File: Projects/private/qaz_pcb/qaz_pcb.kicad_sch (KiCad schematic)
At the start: 77 parts, among them U1 Frood

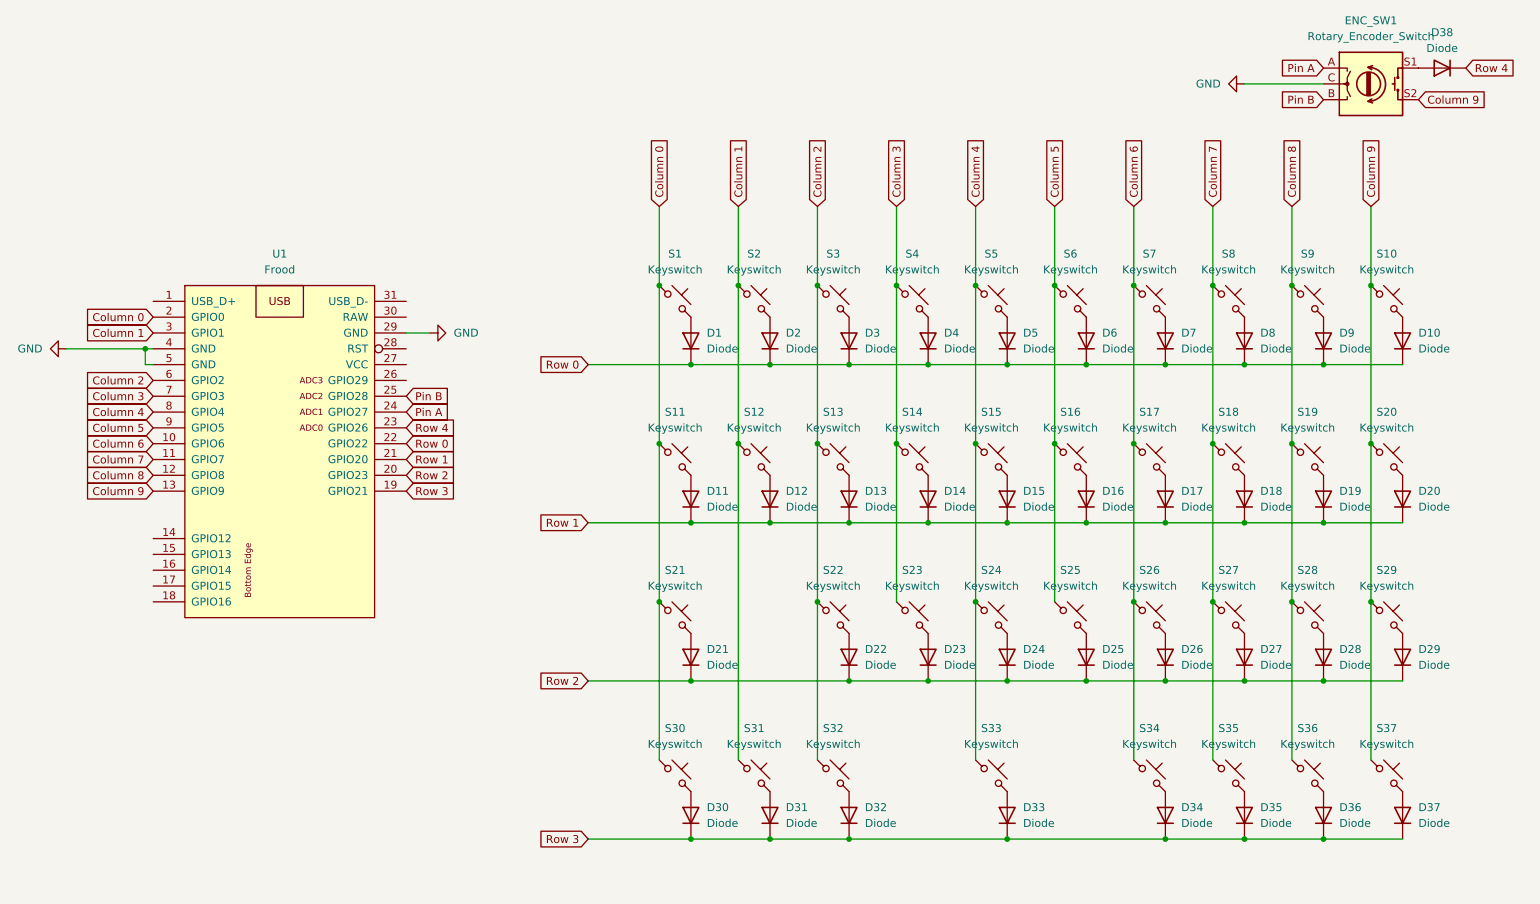
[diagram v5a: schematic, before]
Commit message: Major update
- renamed everything from 'scottokeebs' and 'kunsteak' to 'personal' for easier access and personalisation/individualisation.
- updated README to include sources used in QAZ project
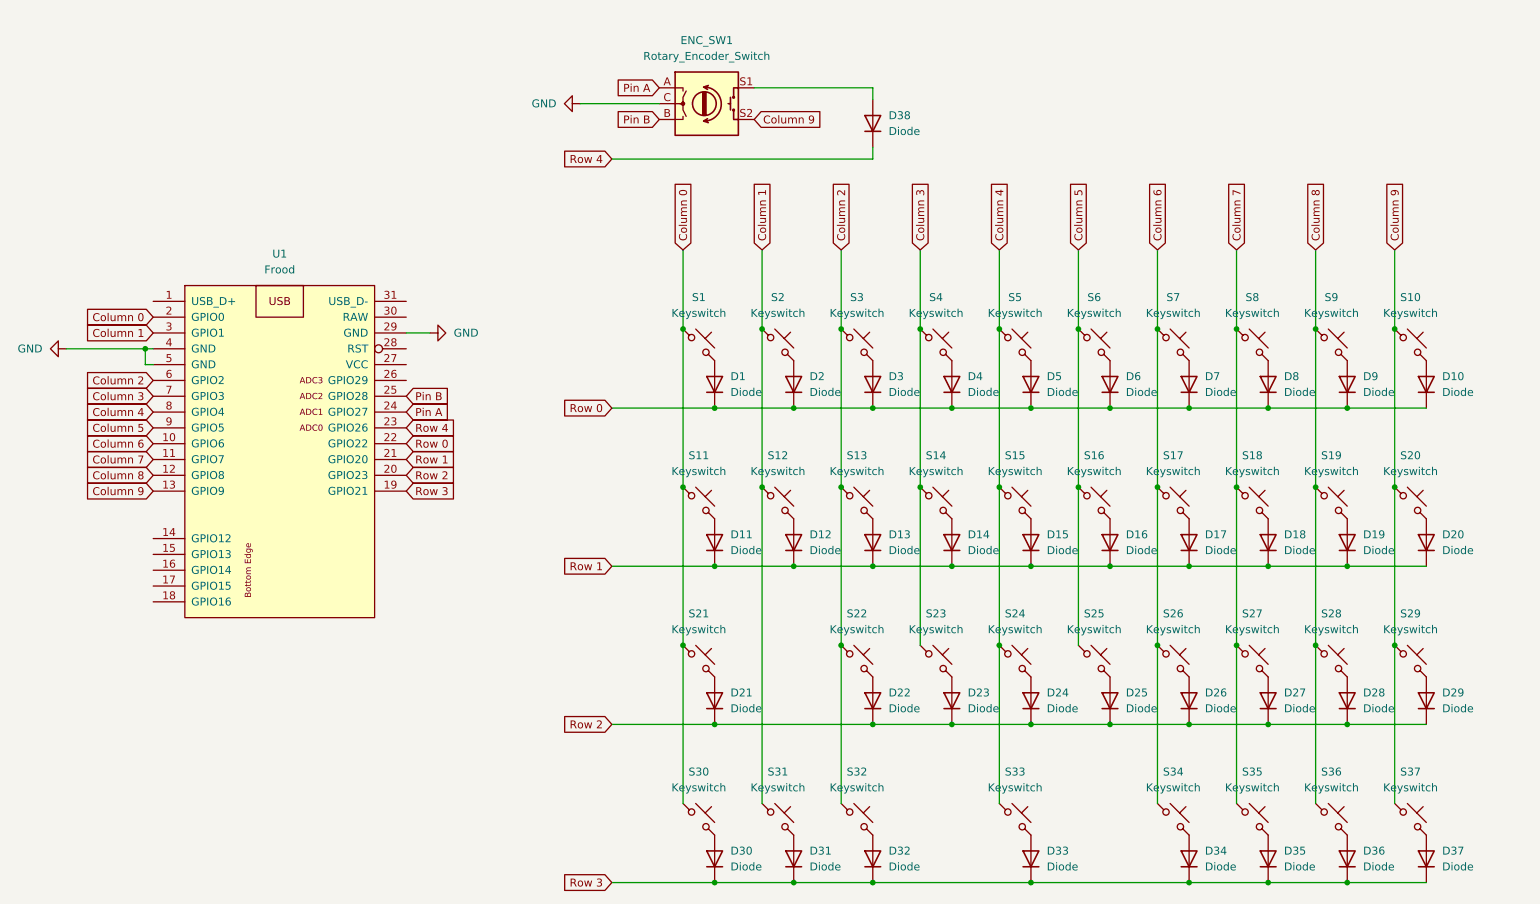
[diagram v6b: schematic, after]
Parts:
- D1, D10, D11, D12, D13, D14, D15, D16, D17, D18, D19, D2, D20, D21, D22, D23, D24, D25, D26, D27, D28, D29, D3, D30, D31, D32, D33, D34, D35, D36, D37, D38, D4, D5, D6, D7, D8, D9: footprint Kunsteak_Components:Diode_SOD-123 -> Personal_Components:Diode_SOD-123; symbol Kunsteak:Placeholder_Diode -> Personal:Placeholder_Diode
- ENC_SW1: footprint Kunsteak_Components:Rotary_Encoder_PEC11R-4220K-S0024 -> Personal_Components:Rotary_Encoder_PEC11R-4220K-S0024; symbol ScottoKeebs:Rotary_Encoder_Switch -> Personal:Rotary_Encoder_Switch
- S1, S12, S13, S14, S15, S16, S17, S18, S19, S2, S20, S22, S23, S24, S25, S26, S27, S28, S29, S3, S30, S31, S32, S35, S36, S37, S4, S5, S6, S7, S8, S9: footprint Kunsteak_Hotswap:Hotswap_MX_1.00u -> Personal_Hotswap:Hotswap_MX_1.00u; symbol Kunsteak:Placeholder_Keyswitch -> Personal:Placeholder_Keyswitch
- S10, S11: footprint Kunsteak_Hotswap:Hotswap_MX_1.25u -> Personal_Hotswap:Hotswap_MX_1.25u; symbol Kunsteak:Placeholder_Keyswitch -> Personal:Placeholder_Keyswitch
- S21: footprint Kunsteak_Hotswap:Hotswap_MX_1.75u -> Personal_Hotswap:Hotswap_MX_1.75u; symbol Kunsteak:Placeholder_Keyswitch -> Personal:Placeholder_Keyswitch
- S33: footprint Kunsteak_Hotswap:Hotswap_MX_2.25u -> Personal_Hotswap:Hotswap_MX_2.25u; symbol Kunsteak:Placeholder_Keyswitch -> Personal:Placeholder_Keyswitch
- S34: footprint Kunsteak_Hotswap:Hotswap_MX_2.00u -> Personal_Hotswap:Hotswap_MX_2.00u; symbol Kunsteak:Placeholder_Keyswitch -> Personal:Placeholder_Keyswitch
- U1: footprint Kunsteak_MCU:Frood_PinHeader_2x13+5_P2.54mm_Labels_Top -> Personal_MCU:Frood_PinHeader_2x13+5_P2.54mm_Labels_Top; symbol ScottoKeebs:Frood -> Personal:Frood
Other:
- moved on the sheet: D1, D10, D11, D12, D13, D14, D15, D16, D17, D18, D19, D2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
